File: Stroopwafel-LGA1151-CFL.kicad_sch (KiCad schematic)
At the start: 0 parts

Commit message: stroopwafel.exe
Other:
- note added: "stroopwafel.exe"

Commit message: nooo they be stealin my stroopwafel
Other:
- note added: "giveitback.png"

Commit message: implemented some misc cpu signals
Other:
- added sheet EC (EC.kicad_sch)
- note added: "15."
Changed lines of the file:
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@@
 		)
 		(fill
-			(type color)
-			(color 255 255 255 1)
+			(type none)
 		)
 	)
@@
 		)
 	)
+	(text "15."
+		(exclude_from_sim no)
+		(at 28.702 132.842 0)
+		(effects
+			(font
+				(size 1.651 1.651)
+				(thickness 0.381)
+				(bold yes)
+				(color 0 0 0 1)
+			)
+		)
+	)
 	(text "File: This one"
 		(exclude_from_sim no)
@@
 	(polyline
 		(pts
+			(xy 26.67 134.62) (xy 116.84 134.62)
+		)
+		(stroke
+			(width 0.635)
+			(type default)
+			(color 116 116 116 1)
+		)
+	)
+	(polyline
+		(pts
 			(xy 226.949 122.809) (xy 253.111 148.971)
 		)
@@
 				)
 			)
+		)
+	)
+	(sheet
+		(at 31.75 130.175)
+		(size 38.1 3.81)
+		(exclude_from_sim no)
+		(in_bom yes)
+		(on_board yes)
+		(dnp no)
+		(stroke
+			(width 0.1524)
+			(type solid)
+		)
+		(fill
+			(color 0 0 0 0.0000)
+		)
+		(property "Sheetname" "EC"
+			(at 31.75 132.715 0)
+			(effects
+				(font
+					(size 1.27 1.27)
+				)
+				(justify left bottom)
+			)
+		)
+		(property "Sheetfile" "EC.kicad_sch"
+			(at 71.12 131.445 0)
+			(effects
+				(font
+					(size 1.27 1.27)
+				)
+				(justify left top)
+			)
+		)
+		(instances
+			(project "Stroopwafel-LGA1151-CFL"
+				(path "/4bc771b8-eb19-46d0-8798-27231a7c6e83"
+					(page "15")
+				)
+			)

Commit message: idek what i changed anymore but there's a bunch of new stuff lol
iirc i did some more misc cpu pins and a bunch of pch pcie stuff
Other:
- added sheet TODO-signals (TODO-signals.kicad_sch)
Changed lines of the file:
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@@
 		(comment 1 "WCFC WC-B551")
 		(comment 3 "stroopwafel for your coffee (lake)")
+		(comment 6 "WCFC? WifiCable Future Center?")
+		(comment 7 "LWFC? Little Wifi Future Center lol")
+		(comment 8 "idk if LCFC would like that.....")
+		(comment 9 "but it would be funny")
 	)
 	(rectangle
@@
 	(rectangle
 		(start 26.035 57.785)
-		(end 117.475 153.67)
+		(end 117.475 154.94)
 		(stroke
 			(width 0.635)
@@
 	(rectangle
 		(start 25.4 50.8)
-		(end 118.11 154.305)
+		(end 118.11 155.575)
 		(stroke
 			(width 0.635)
@@
 	(polyline
 		(pts
+			(xy 26.67 149.86) (xy 116.84 149.86)
+		)
+		(stroke
+			(width 0.635)
+			(type default)
+			(color 116 116 116 1)
+		)
+	)
+	(polyline
+		(pts
 			(xy 26.67 73.66) (xy 116.84 73.66)
 		)
@@
 	(polyline
 		(pts
+			(xy 26.67 139.7) (xy 116.84 139.7)
+		)
+		(stroke
+			(width 0.635)
+			(type default)
+			(color 116 116 116 1)
+		)
+	)
+	(polyline
+		(pts
 			(xy 26.67 124.46) (xy 116.84 124.46)
 		)
@@
 	(polyline
 		(pts
+			(xy 26.67 144.78) (xy 116.84 144.78)
+		)
+		(stroke
+			(width 0.635)
+			(type default)
+			(color 116 116 116 1)
+		)
+	)
+	(polyline
+		(pts
 			(xy 253.111 129.159) (xy 226.949 155.321)
 		)
@@
 	(polyline
 		(pts
-			(xy 70.485 58.42) (xy 70.485 153.035)
+			(xy 70.485 58.42) (xy 70.485 154.305)
 		)
 		(stroke
@@
 	(polyline
 		(pts
-			(xy 31.115 58.42) (xy 31.115 153.035)
+			(xy 31.115 58.42) (xy 31.115 154.305)
 		)
 		(stroke
@@
 				)
 			)
+		)
+	)
+	(sheet
+		(at 31.75 150.495)
+		(size 38.1 3.81)
+		(exclude_from_sim no)
+		(in_bom yes)
+		(on_board yes)
+		(dnp no)
+		(stroke
+			(width 0.1524)
+			(type solid)
+		)
+		(fill
+			(color 0 0 0 0.0000)
+		)
+		(property "Sheetname" "TODO-signals"
+			(at 31.75 153.035 0)
+			(effects
+				(font
+					(size 1.27 1.27)
+				)
+				(justify left bottom)
+			)
+		)
+		(property "Sheetfile" "TODO-signals.kicad_sch"
+			(at 71.12 151.765 0)
+			(effects
+				(font
+					(size 1.27 1.27)
+				)
+				(justify left top)
+			)
+		)
+		(instances
+			(project "Stroopwafel-LGA1151-CFL"
+				(path "/4bc771b8-eb19-46d0-8798-27231a7c6e83"
+					(page "20")
+				)
+			)

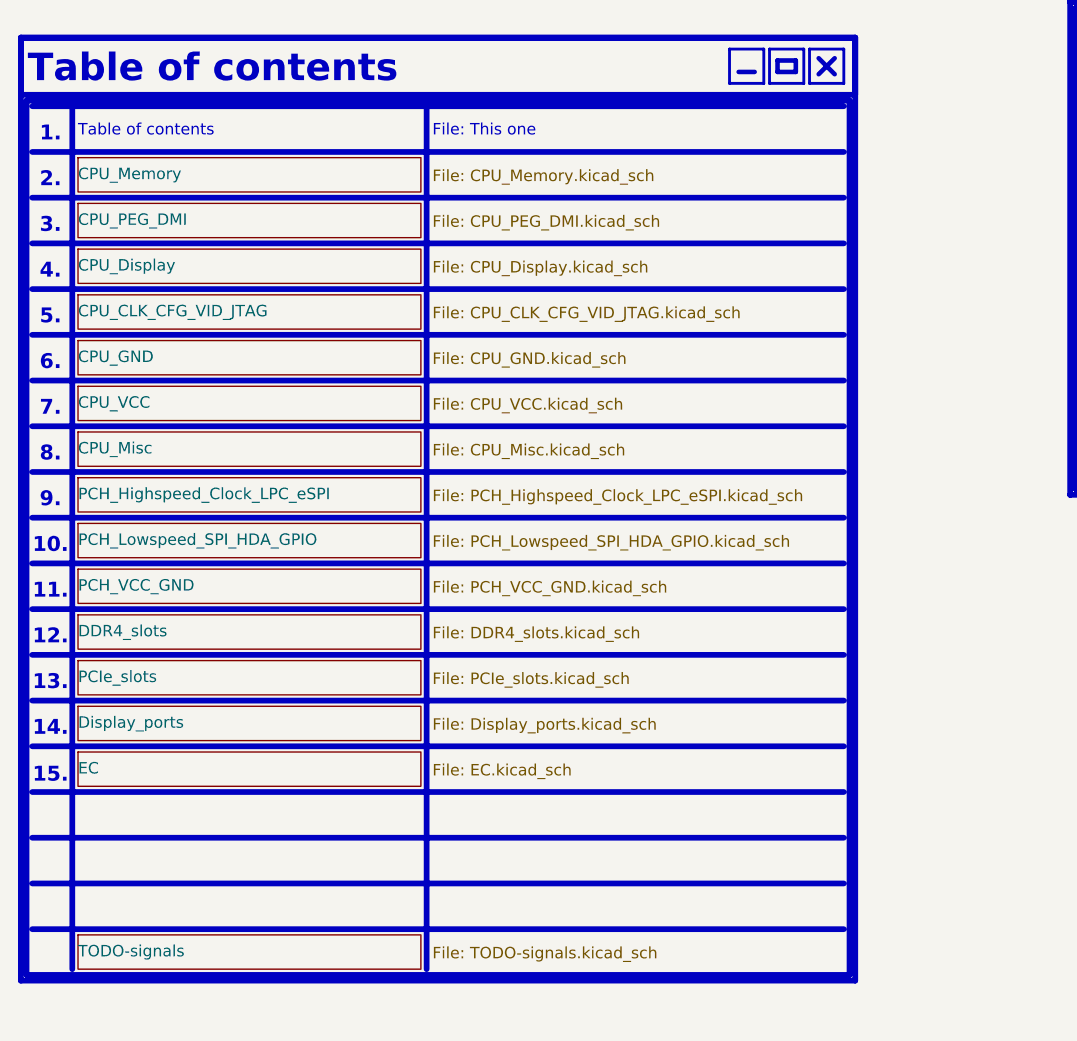
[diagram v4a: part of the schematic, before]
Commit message: Restructured schematic
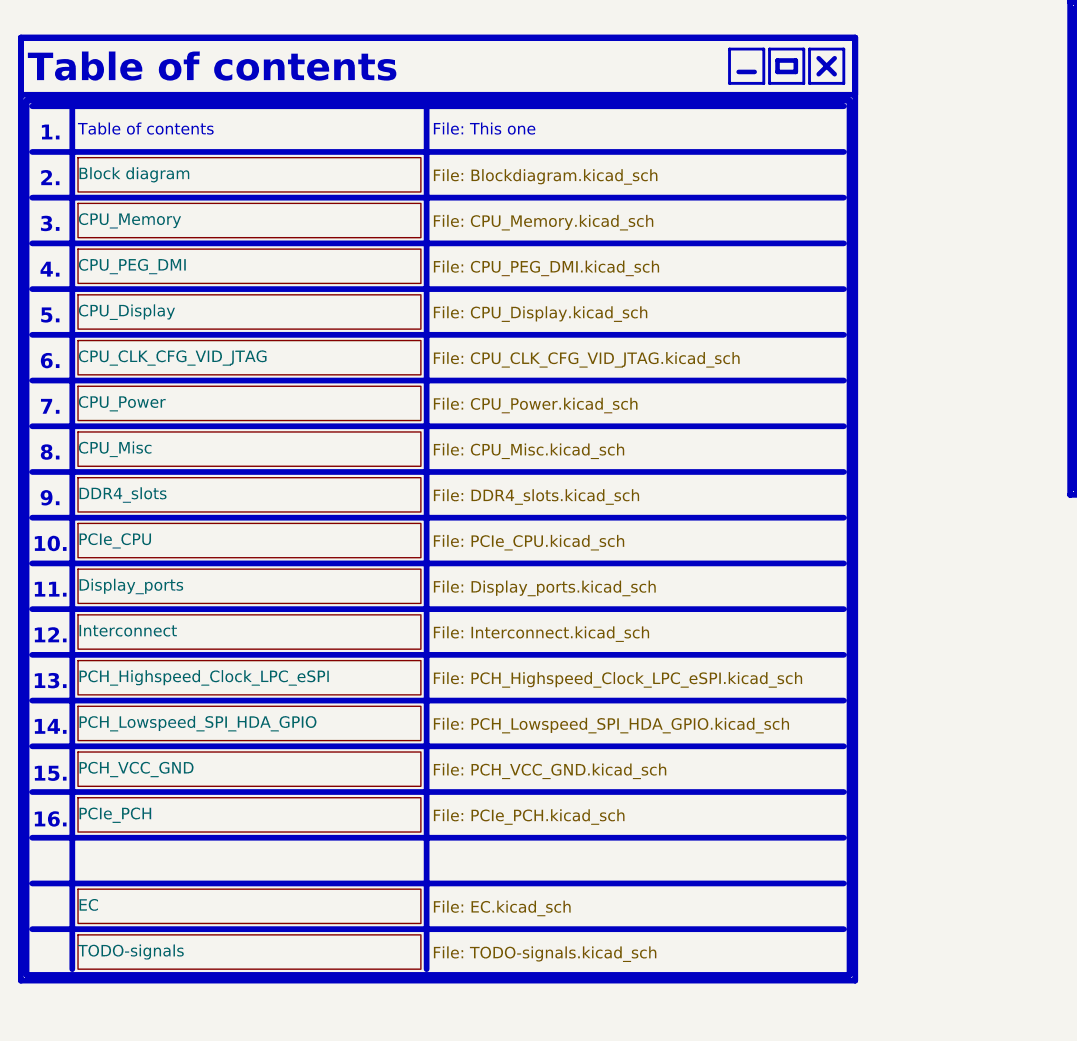
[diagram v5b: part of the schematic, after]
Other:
- removed sheet CPU_GND
- removed sheet CPU_VCC
- removed sheet PCIe_slots
- added sheet Block diagram (Blockdiagram.kicad_sch)
- added sheet CPU_Power (CPU_Power.kicad_sch)
- added sheet Interconnect (Interconnect.kicad_sch)
- added sheet PCIe_CPU (PCIe_CPU.kicad_sch)
- added sheet PCIe_PCH (PCIe_PCH.kicad_sch)
- note added: "16."
